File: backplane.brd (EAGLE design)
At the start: 153.7 x 128.3 mm, 71 parts, among them J1 L717HDE15PD4CH4R, J10 5013310807, J11 5013310807, J12 5013310807, J13 5013310807, J14 5013311007, J15 5013311007, J16 5013311007, J17 5013311007, J18 5013311007, J19 5013311007, J2 1054301102, J20 5013311007, J21 5013311007, J22 5013311007, J23 5013311007, J24 SEAM-40-03.0-S-06-2-A-K-TR, J25 5055670271, J26 SAMTEC-TST-110-01-X-DJ, J27 SAMTEC-TST-110-01-X-DJ, J28 SAMTEC-TST-110-01-X-DJ, J29 SAMTEC-TST-110-01-X-DJ, J3 5011902017, J4 5013310807, J5 5013310807, J6 5013310807, J7 5013310807, J8 5013310807, J9 5013310807, U1 AM26LV32EIPWR, U10 AM26LV32EIPWR, U11 LP3962EMP-3.3, U2 AM26LV32EIPWR, U3 AM26LV32EIPWR, U4 AM26LV32EIPWR, U5 AM26LV32EIPWR, U6 AM26LV32EIPWR, U7 AM26LV32EIPWR, U8 AM26LV32EIPWR, U9 AM26LV32EIPWR

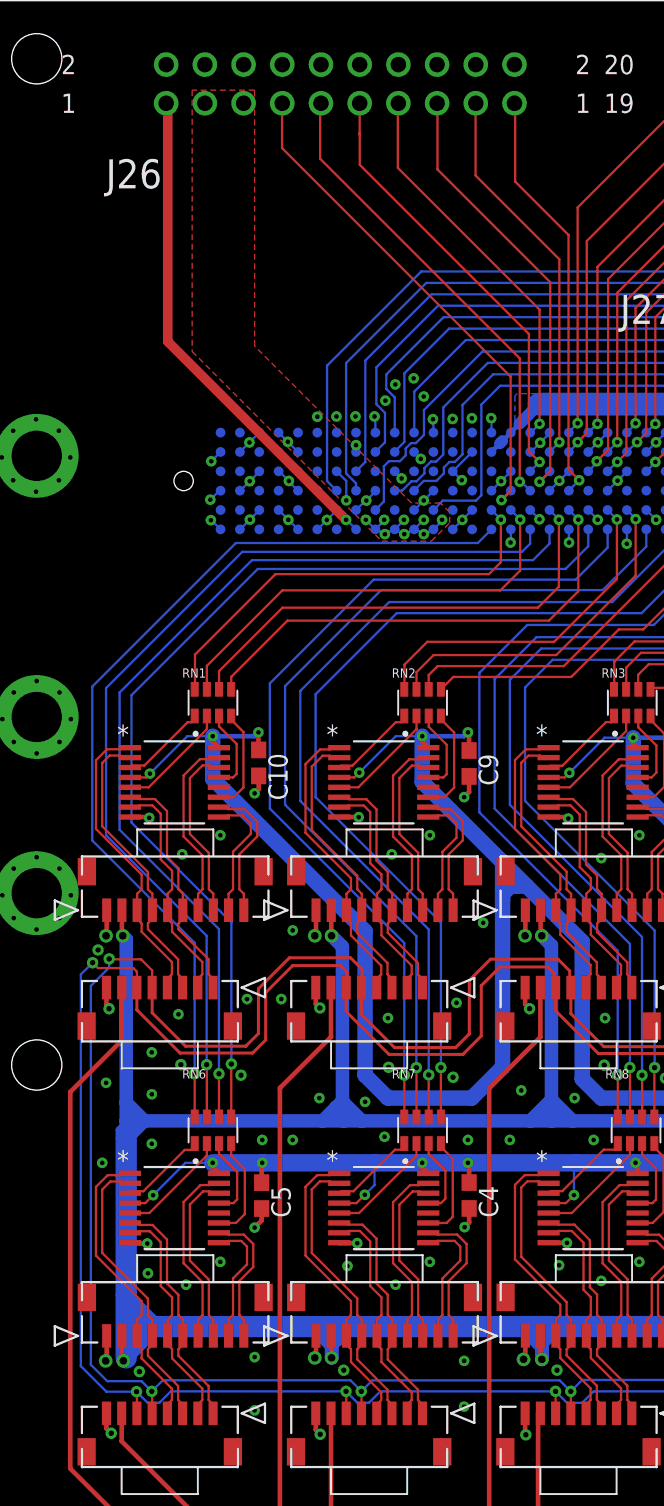
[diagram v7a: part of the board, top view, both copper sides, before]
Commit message: DRC Checks passed, in-depth review INCOMPLETE
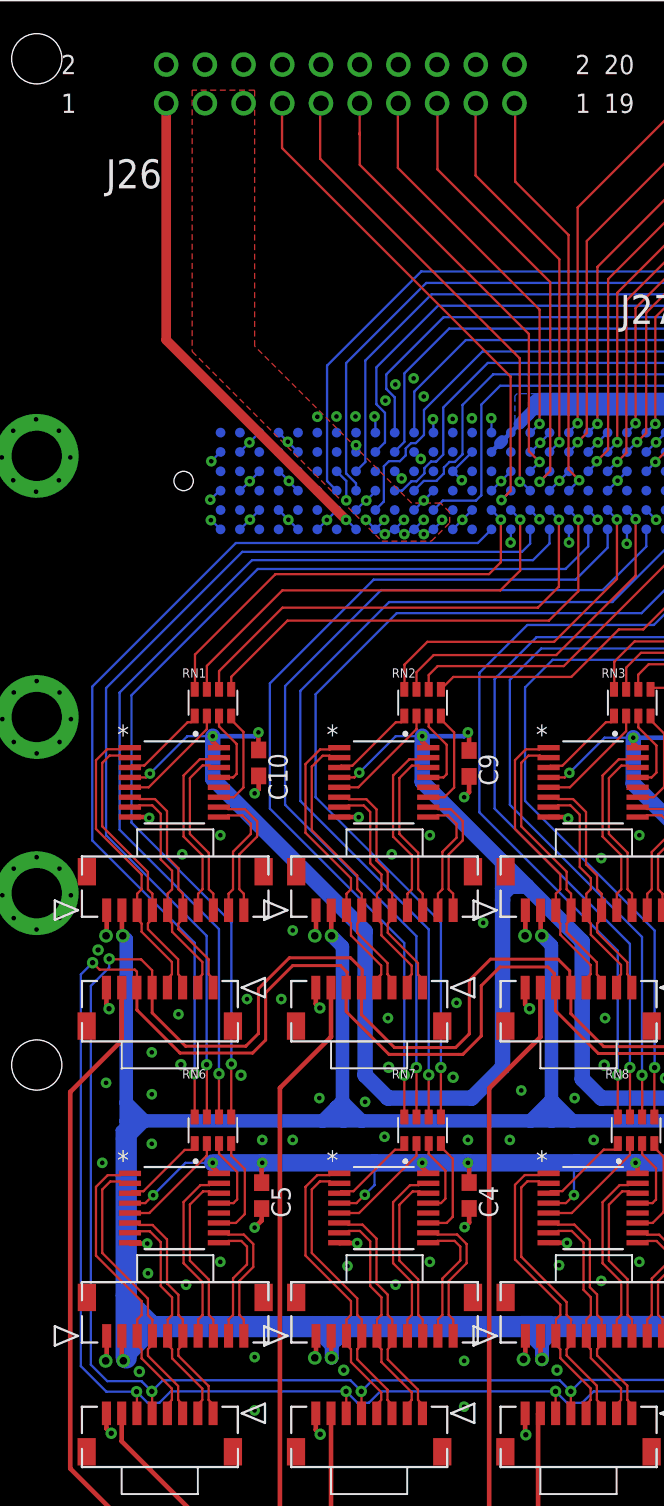
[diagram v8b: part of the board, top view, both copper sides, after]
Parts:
- C1, C10, C2, C3, C4, C5, C6, C7, C8, C9: value (none) -> 0.1uF
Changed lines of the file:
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@@
 <attribute name="NAME" x="75.5938" y="0.635" size="1.27" layer="27" ratio="6" rot="SR0"/>
 </element>
-<element name="C1" library="rcl" library_urn="urn:adsk.eagle:library:334" package="C0603" package3d_urn="urn:adsk.eagle:package:23616/2" value="" x="72.91" y="49.995" smashed="yes" rot="R270">
+<element name="C1" library="rcl" library_urn="urn:adsk.eagle:library:334" package="C0603" package3d_urn="urn:adsk.eagle:package:23616/2" value="0.1uF" x="72.91" y="49.995" smashed="yes" rot="R270">
 <attribute name="NAME" x="73.545" y="50.63" size="1.27" layer="25" rot="R270"/>
 <attribute name="POPULARITY" value="73" x="72.91" y="49.995" size="6" layer="27" rot="R270" display="off"/>
@@
 <attribute name="VALUE" x="71.005" y="50.63" size="1.27" layer="27" rot="R270"/>
 </element>
-<element name="C2" library="rcl" library_urn="urn:adsk.eagle:library:334" package="C0603" package3d_urn="urn:adsk.eagle:package:23616/2" value="" x="59.185" y="49.785" smashed="yes" rot="R270">
+<element name="C2" library="rcl" library_urn="urn:adsk.eagle:library:334" package="C0603" package3d_urn="urn:adsk.eagle:package:23616/2" value="0.1uF" x="59.185" y="49.785" smashed="yes" rot="R270">
 <attribute name="NAME" x="59.82" y="50.42" size="1.27" layer="25" rot="R270"/>
 <attribute name="POPULARITY" value="73" x="59.185" y="49.785" size="6" layer="27" rot="R270" display="off"/>
@@
 <attribute name="VALUE" x="57.28" y="50.42" size="1.27" layer="27" rot="R270"/>
 </element>
-<element name="C3" library="rcl" library_urn="urn:adsk.eagle:library:334" package="C0603" package3d_urn="urn:adsk.eagle:package:23616/2" value="" x="45.405" y="49.725" smashed="yes" rot="R270">
+<element name="C3" library="rcl" library_urn="urn:adsk.eagle:library:334" package="C0603" package3d_urn="urn:adsk.eagle:package:23616/2" value="0.1uF" x="45.405" y="49.725" smashed="yes" rot="R270">
 <attribute name="NAME" x="46.04" y="50.36" size="1.27" layer="25" rot="R270"/>
 <attribute name="POPULARITY" value="73" x="45.405" y="49.725" size="6" layer="27" rot="R270" display="off"/>
@@
 <attribute name="VALUE" x="43.5" y="50.36" size="1.27" layer="27" rot="R270"/>
 </element>
-<element name="C4" library="rcl" library_urn="urn:adsk.eagle:library:334" package="C0603" package3d_urn="urn:adsk.eagle:package:23616/2" value="" x="31.58" y="49.855" smashed="yes" rot="R270">
+<element name="C4" library="rcl" library_urn="urn:adsk.eagle:library:334" package="C0603" package3d_urn="urn:adsk.eagle:package:23616/2" value="0.1uF" x="31.58" y="49.855" smashed="yes" rot="R270">
 <attribute name="NAME" x="32.215" y="50.49" size="1.27" layer="25" rot="R270"/>
 <attribute name="POPULARITY" value="73" x="31.58" y="49.855" size="6" layer="27" rot="R270" display="off"/>
@@
 <attribute name="VALUE" x="29.675" y="50.49" size="1.27" layer="27" rot="R270"/>
 </element>
-<element name="C5" library="rcl" library_urn="urn:adsk.eagle:library:334" package="C0603" package3d_urn="urn:adsk.eagle:package:23616/2" value="" x="17.96" y="49.85" smashed="yes" rot="R270">
+<element name="C5" library="rcl" library_urn="urn:adsk.eagle:library:334" package="C0603" package3d_urn="urn:adsk.eagle:package:23616/2" value="0.1uF" x="17.96" y="49.85" smashed="yes" rot="R270">
 <attribute name="NAME" x="18.595" y="50.485" size="1.27" layer="25" rot="R270"/>
 <attribute name="POPULARITY" value="73" x="17.96" y="49.85" size="6" layer="27" rot="R270" display="off"/>
@@
 <attribute name="VALUE" x="16.055" y="50.485" size="1.27" layer="27" rot="R270"/>
 </element>
-<element name="C6" library="rcl" library_urn="urn:adsk.eagle:library:334" package="C0603" package3d_urn="urn:adsk.eagle:package:23616/2" value="" x="73" y="77.5" smashed="yes" rot="R270">
+<element name="C6" library="rcl" library_urn="urn:adsk.eagle:library:334" package="C0603" package3d_urn="urn:adsk.eagle:package:23616/2" value="0.1uF" x="73" y="77.5" smashed="yes" rot="R270">
 <attribute name="NAME" x="73.635" y="78.135" size="1.27" layer="25" rot="R270"/>
 <attribute name="POPULARITY" value="73" x="73" y="77.5" size="6" layer="27" rot="R270" display="off"/>
@@
 <attribute name="VALUE" x="71.095" y="78.135" size="1.27" layer="27" rot="R270"/>
 </element>
-<element name="C7" library="rcl" library_urn="urn:adsk.eagle:library:334" package="C0603" package3d_urn="urn:adsk.eagle:package:23616/2" value="" x="59.15" y="78.285" smashed="yes" rot="R270">
+<element name="C7" library="rcl" library_urn="urn:adsk.eagle:library:334" package="C0603" package3d_urn="urn:adsk.eagle:package:23616/2" value="0.1uF" x="59.15" y="78.285" smashed="yes" rot="R270">
 <attribute name="NAME" x="59.785" y="78.92" size="1.27" layer="25" rot="R270"/>
 <attribute name="POPULARITY" value="73" x="59.15" y="78.285" size="6" layer="27" rot="R270" display="off"/>
@@
 <attribute name="VALUE" x="57.245" y="78.92" size="1.27" layer="27" rot="R270"/>
 </element>
-<element name="C8" library="rcl" library_urn="urn:adsk.eagle:library:334" package="C0603" package3d_urn="urn:adsk.eagle:package:23616/2" value="" x="45.38" y="78.155" smashed="yes" rot="R270">
+<element name="C8" library="rcl" library_urn="urn:adsk.eagle:library:334" package="C0603" package3d_urn="urn:adsk.eagle:package:23616/2" value="0.1uF" x="45.38" y="78.155" smashed="yes" rot="R270">
 <attribute name="NAME" x="46.015" y="78.79" size="1.27" layer="25" rot="R270"/>
 <attribute name="POPULARITY" value="73" x="45.38" y="78.155" size="6" layer="27" rot="R270" display="off"/>
@@
 <attribute name="VALUE" x="43.475" y="78.79" size="1.27" layer="27" rot="R270"/>
 </element>
-<element name="C9" library="rcl" library_urn="urn:adsk.eagle:library:334" package="C0603" package3d_urn="urn:adsk.eagle:package:23616/2" value="" x="31.575" y="78.21" smashed="yes" rot="R270">
+<element name="C9" library="rcl" library_urn="urn:adsk.eagle:library:334" package="C0603" package3d_urn="urn:adsk.eagle:package:23616/2" value="0.1uF" x="31.575" y="78.21" smashed="yes" rot="R270">
 <attribute name="NAME" x="32.21" y="78.845" size="1.27" layer="25" rot="R270"/>
 <attribute name="POPULARITY" value="73" x="31.575" y="78.21" size="6" layer="27" rot="R270" display="off"/>
@@
 <attribute name="VALUE" x="29.67" y="78.845" size="1.27" layer="27" rot="R270"/>
 </element>
-<element name="C10" library="rcl" library_urn="urn:adsk.eagle:library:334" package="C0603" package3d_urn="urn:adsk.eagle:package:23616/2" value="" x="17.765" y="78.245" smashed="yes" rot="R270">
+<element name="C10" library="rcl" library_urn="urn:adsk.eagle:library:334" package="C0603" package3d_urn="urn:adsk.eagle:package:23616/2" value="0.1uF" x="17.765" y="78.245" smashed="yes" rot="R270">
 <attribute name="NAME" x="18.4" y="78.88" size="1.27" layer="25" rot="R270"/>
 <attribute name="POPULARITY" value="73" x="17.765" y="78.245" size="6" layer="27" rot="R270" display="off"/>
@@
 <wire x1="65.735" y1="33.765" x2="65.735" y2="35.56" width="0.1524" layer="1"/>
 <wire x1="71.84" y1="27.66" x2="65.735" y2="33.765" width="0.1524" layer="1"/>
-<wire x1="38.255" y1="35.56" x2="38.28" y2="35.525" width="0" layer="19" extent="1-1"/>
+<wire x1="38.255" y1="35.56" x2="38.28" y2="35.535" width="0.1524" layer="1"/>
+<wire x1="38.28" y1="35.535" x2="38.28" y2="35.525" width="0.1524" layer="1"/>
 </signal>
 <signal name="ESTP-">
@@
 <wire x1="6.0922" y1="64.3622" x2="6.0922" y2="38.6578" width="0.1524" layer="16"/>
 <wire x1="9.775" y1="63.5" x2="9.775" y2="64.545" width="0.1524" layer="1"/>
-<wire x1="9.775" y1="64.545" x2="9.54" y2="64.78" width="0.1524" layer="1"/>
-<wire x1="9.54" y1="64.78" x2="7.22" y2="64.78" width="0.1524" layer="1"/>
-<wire x1="7.22" y1="64.78" x2="6.865" y2="65.135" width="0.1524" layer="1"/>
+<wire x1="9.775" y1="64.545" x2="9.64" y2="64.68" width="0.1524" layer="1"/>
+<wire x1="9.64" y1="64.68" x2="7.32" y2="64.68" width="0.1524" layer="1"/>
+<wire x1="7.32" y1="64.68" x2="6.865" y2="65.135" width="0.1524" layer="1"/>
 <wire x1="9.75" y1="36.98" x2="10.48" y2="36.25" width="0.1524" layer="16"/>
 <wire x1="10.48" y1="36.25" x2="11.25" y2="36.25" width="0.1524" layer="16"/>
@@
 <wire x1="23.5304" y1="94.2" x2="23.5" y2="94.2" width="0.1524" layer="16"/>
 <via x="23.5" y="94.2" extent="1-16" drill="0.3"/>
-<wire x1="23.5" y1="94.2" x2="11.8" y2="105.9" width="0.635" layer="1"/>
-<wire x1="11.8" y1="105.9" x2="11.8" y2="122" width="0.635" layer="1"/>
+<wire x1="23.5" y1="94.2" x2="11.695" y2="106.005" width="0.635" layer="1"/>
+<wire x1="11.695" y1="121.22" x2="11.695" y2="106.005" width="0.635" layer="1"/>
 <contactref element="J26" pad="1"/>
-<wire x1="11.8" y1="122" x2="11.695" y2="121.540009375" width="0" layer="19" extent="1-1"/>
+<wire x1="11.695" y1="121.540009375" x2="11.695" y2="121.22" width="0.1524" layer="1"/>
 </signal>
 <signal name="5V_SBRIO">
@@
 <mfgpreviewcolor name="substratecolor" color="0xFF786E46"/>
 </mfgpreviewcolors>
+<errors>
+</errors>
 </board>
 </drawing>
